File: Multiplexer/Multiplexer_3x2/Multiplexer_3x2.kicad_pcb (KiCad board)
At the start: 2 copper layers, 36.8 x 128 mm, 12 parts, among them J1 In1, J2 Out1, J3 Out1, J4 In2, J5 Out2, J6 Out2, J7 In3, J8 Out3, J9 Out3

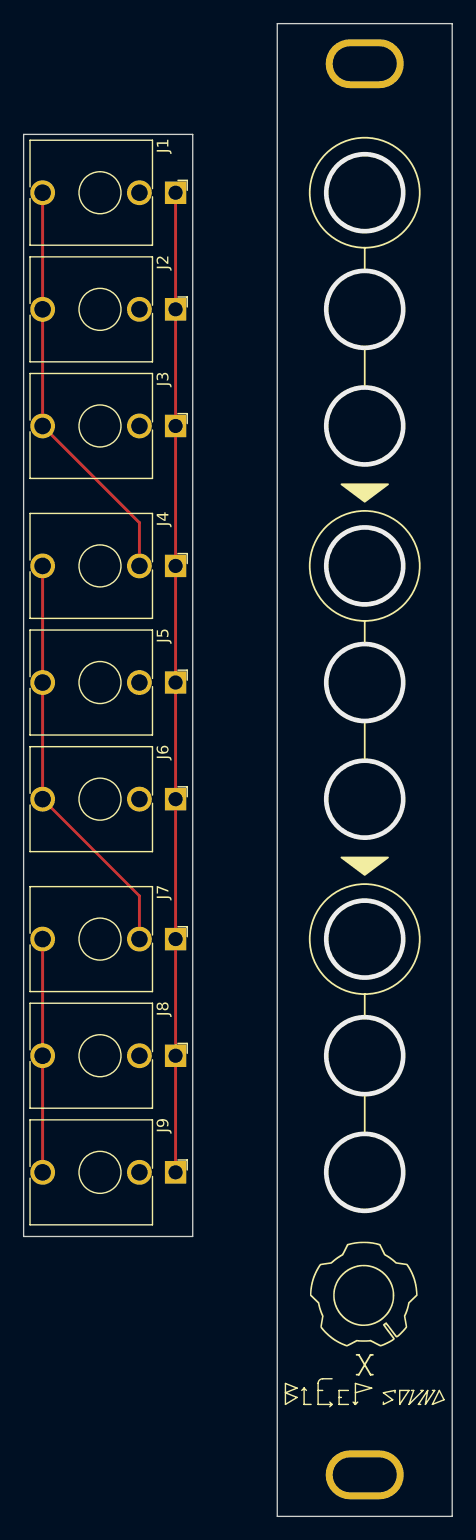
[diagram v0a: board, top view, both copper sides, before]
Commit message: fix position of mounting holes for front
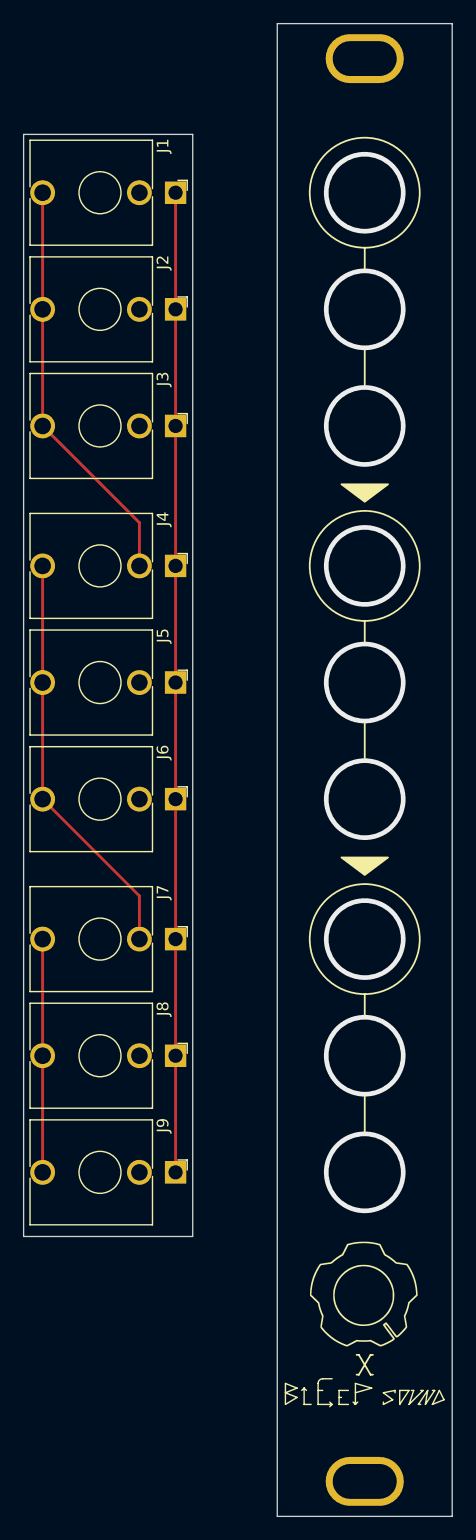
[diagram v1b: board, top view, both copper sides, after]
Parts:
- moved H1 0.56 mm to (82.0, 152.5)
- moved H2 0.44 mm to (82.0, 30.5)
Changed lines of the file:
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@@
   )
   (footprint "Synth:Doepfer Mounting hole" (layer "F.Cu")
-    (at 82 30.939511)
+    (at 82 30.5)
     (property "Sheetfile" "Multiplexer_3x2.kicad_sch")
     (property "Sheetname" "")
@@
   )
   (footprint "Synth:Doepfer Mounting hole" (layer "F.Cu")
-    (at 82 151.939511)
+    (at 82 152.5)
     (property "Sheetfile" "Multiplexer_3x2.kicad_sch")
     (property "Sheetname" "")

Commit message: Add iftec logo to multiplexer
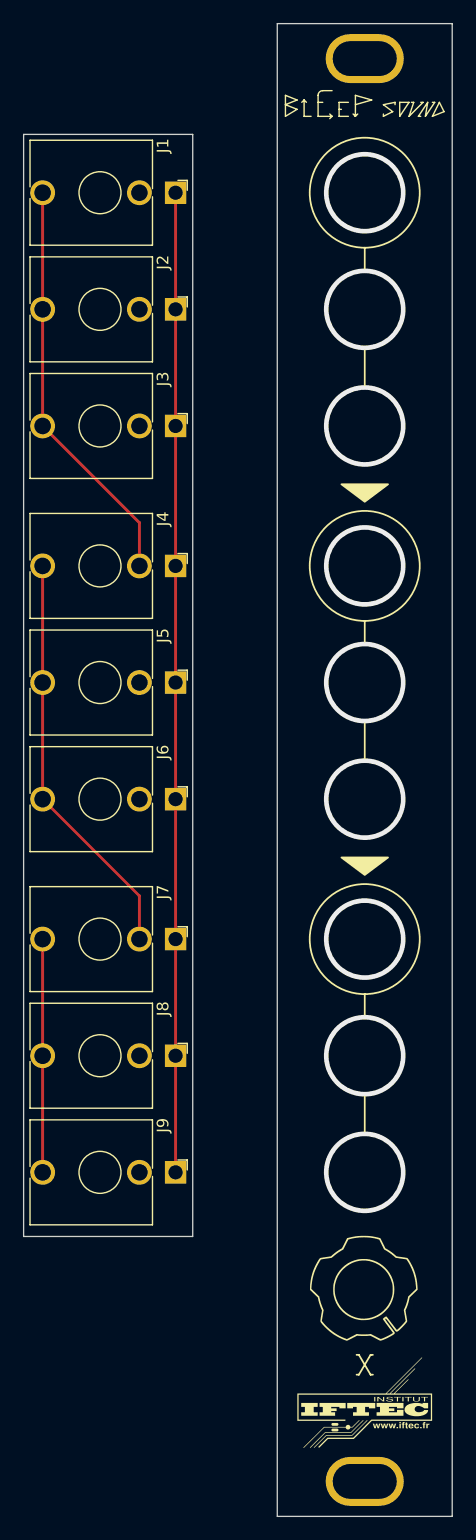
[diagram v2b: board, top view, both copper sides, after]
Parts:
- added G***: LOGO, LOGO, F.Cu at (82.0, 145.8)
- moved G*** 0.50 mm to (82.0, 136.0)
